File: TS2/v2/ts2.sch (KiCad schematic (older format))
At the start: 4 parts

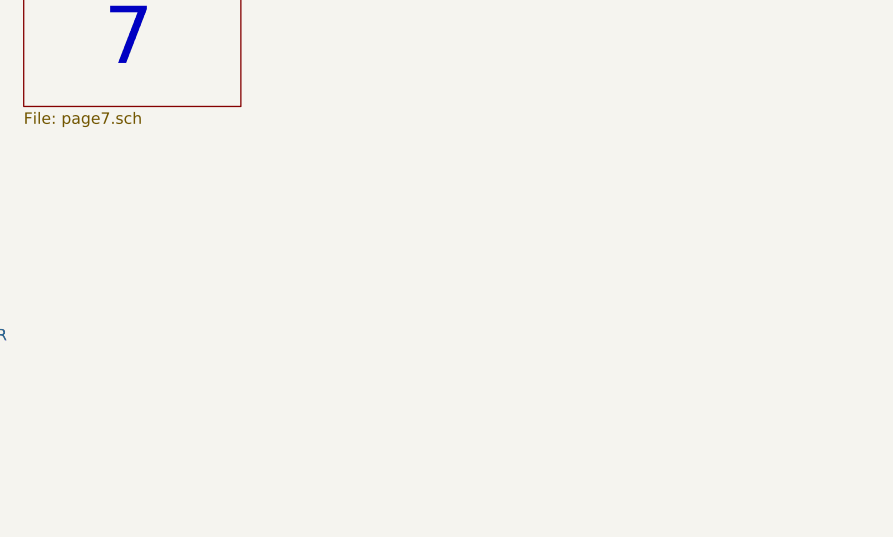
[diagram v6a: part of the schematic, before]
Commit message: ELiminated one chip (U28) by using other unused gates. Added unused gates to schematic.
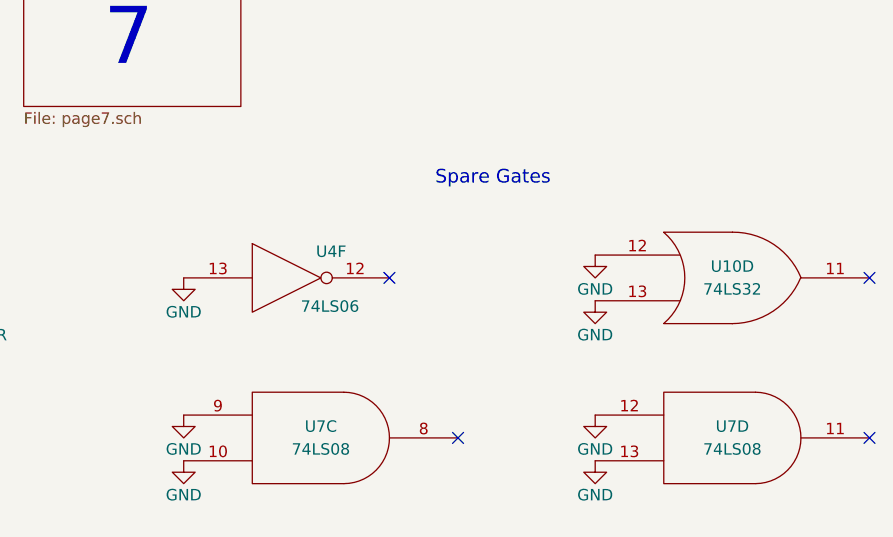
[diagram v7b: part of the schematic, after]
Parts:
- added U10: 74LS32, symbol 74LS32
- added U4: 74LS06, symbol 74LS06
- added U7: 74LS08, symbol 74LS08
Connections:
- net GND: now also U10.12, U10.13, U10.7 (GND), U4.13, U4.7 (GND), U7.10, U7.12, U7.13, U7.7 (GND), U7.7 (GND), U7.9
- net VCC: now also U10.14 (VCC), U4.14 (VCC), U7.14 (VCC), U7.14 (VCC)
- no-connect marks 0 -> 4
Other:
- note added: "Spare Gates"
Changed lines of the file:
@@
 Wire Wire Line
 	4300 5050 4300 5150
+Text Notes 6500 4200 0    60   ~ 0
+Spare Gates
+$Comp
+L 74LS06 U4
+U 6 1 58430894
+P 5850 4600
+F 0 "U4" H 6045 4715 50  0000 C CNN
+F 1 "74LS06" H 6040 4475 50  0000 C CNN
+F 2 "" H 5850 4600 50  0000 C CNN
+F 3 "" H 5850 4600 50  0000 C CNN
+	6    5850 4600
+	1    0    0    -1
+$EndComp
+$Comp
+L 74LS08 U7
+U 3 1 58430C38
+P 6000 5300
+F 0 "U7" H 6000 5350 50  0000 C CNN
+F 1 "74LS08" H 6000 5250 50  0000 C CNN
+F 2 "" H 6000 5300 50  0000 C CNN
+F 3 "" H 6000 5300 50  0000 C CNN
+	3    6000 5300
+	1    0    0    -1
+$EndComp
+$Comp
+L 74LS08 U7
+U 4 1 58430C82
+P 7800 5300
+F 0 "U7" H 7800 5350 50  0000 C CNN
+F 1 "74LS08" H 7800 5250 50  0000 C CNN
+F 2 "" H 7800 5300 50  0000 C CNN
+F 3 "" H 7800 5300 50  0000 C CNN
+	4    7800 5300
+	1    0    0    -1
+$EndComp
+$Comp
+L 74LS32 U10
+U 4 1 5843109B
+P 7800 4600
+F 0 "U10" H 7800 4650 50  0000 C CNN
+F 1 "74LS32" H 7800 4550 50  0000 C CNN
+F 2 "" H 7800 4600 50  0000 C CNN
+F 3 "" H 7800 4600 50  0000 C CNN
+	4    7800 4600
+	1    0    0    -1
+$EndComp
+NoConn ~ 8400 4600
+NoConn ~ 8400 5300
+NoConn ~ 6600 5300
+NoConn ~ 6300 4600
+$Comp
+L GND #PWR011
+U 1 1 58432036
+P 5400 4600
+F 0 "#PWR011" H 5400 4350 50  0001 C CNN
+F 1 "GND" H 5400 4450 50  0000 C CNN
+F 2 "" H 5400 4600 50  0000 C CNN
+F 3 "" H 5400 4600 50  0000 C CNN
+	1    5400 4600
+	1    0    0    -1
+$EndComp
+$Comp
+L GND #PWR012
+U 1 1 584320D8
+P 5400 5200
+F 0 "#PWR012" H 5400 4950 50  0001 C CNN
+F 1 "GND" H 5400 5050 50  0000 C CNN
+F 2 "" H 5400 5200 50  0000 C CNN
+F 3 "" H 5400 5200 50  0000 C CNN
+	1    5400 5200
+	1    0    0    -1
+$EndComp
+$Comp
+L GND #PWR013
+U 1 1 584320FC
+P 5400 5400
+F 0 "#PWR013" H 5400 5150 50  0001 C CNN
+F 1 "GND" H 5400 5250 50  0000 C CNN
+F 2 "" H 5400 5400 50  0000 C CNN
+F 3 "" H 5400 5400 50  0000 C CNN
+	1    5400 5400
+	1    0    0    -1
+$EndComp
+$Comp
+L GND #PWR014
+U 1 1 584321C8
+P 7200 4500
+F 0 "#PWR014" H 7200 4250 50  0001 C CNN
+F 1 "GND" H 7200 4350 50  0000 C CNN
+F 2 "" H 7200 4500 50  0000 C CNN
+F 3 "" H 7200 4500 50  0000 C CNN
+	1    7200 4500
+	1    0    0    -1
+$EndComp
+$Comp
+L GND #PWR015
+U 1 1 584321EC
+P 7200 4700
+F 0 "#PWR015" H 7200 4450 50  0001 C CNN
+F 1 "GND" H 7200 4550 50  0000 C CNN
+F 2 "" H 7200 4700 50  0000 C CNN
+F 3 "" H 7200 4700 50  0000 C CNN
+	1    7200 4700
+	1    0    0    -1
+$EndComp
+$Comp
+L GND #PWR016
+U 1 1 58432210
+P 7200 5200
+F 0 "#PWR016" H 7200 4950 50  0001 C CNN
+F 1 "GND" H 7200 5050 50  0000 C CNN
+F 2 "" H 7200 5200 50  0000 C CNN
+F 3 "" H 7200 5200 50  0000 C CNN
+	1    7200 5200
+	1    0    0    -1
+$EndComp
+$Comp
+L GND #PWR017
+U 1 1 58432234
+P 7200 5400
+F 0 "#PWR017" H 7200 5150 50  0001 C CNN
+F 1 "GND" H 7200 5250 50  0000 C CNN
+F 2 "" H 7200 5400 50  0000 C CNN
+F 3 "" H 7200 5400 50  0000 C CNN
+	1    7200 5400
+	1    0    0    -1
+$EndComp
 $EndSCHEMATC
